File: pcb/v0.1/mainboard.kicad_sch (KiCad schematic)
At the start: 11 parts, among them J1 Conn_01x02_Pin, J2 TYPE_C_Receptacle, J3 Conn_01x04_Pin, U1 AP2112K-3.3TRG1

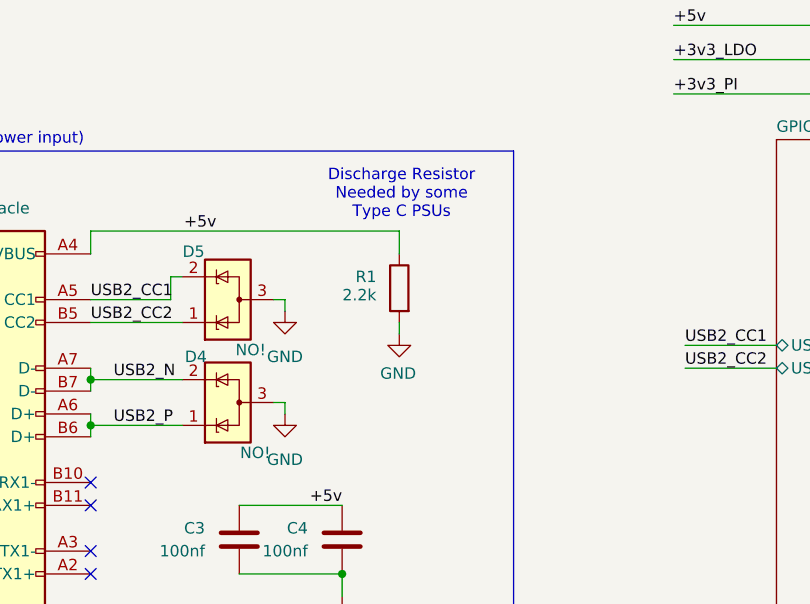
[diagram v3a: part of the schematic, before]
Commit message: Finish ESD protection.
There are now TVS diodes/arrays on both the signal lines and power lines
in every user accessible connector. Such as USBc ports and GPIO.

I have not included them for internal headers, jumpers or connectors
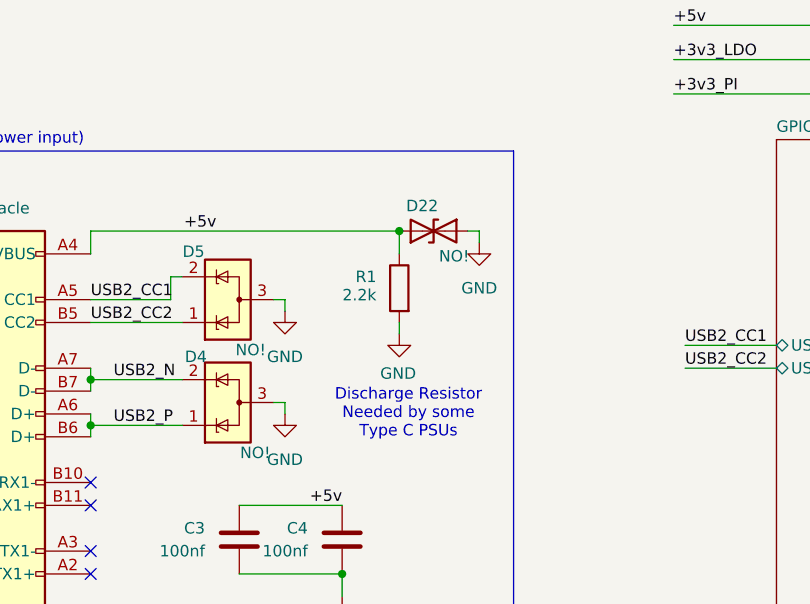
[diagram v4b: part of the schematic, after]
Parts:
- added D22: TVS_DIODE_7.1VC, Diode_SMD:D_SOD-882, symbol TH-1-CC:TVS_DIODE_7.1VC
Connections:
- net +5v: now also D22.1 (A1)
- net GND: now also D22.2 (A2)
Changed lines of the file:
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@@
 	(text "Discharge Resistor\nNeeded by some\nType C PSUs"
 		(exclude_from_sim no)
-		(at 84.074 34.036 0)
+		(at 84.836 58.42 0)
 		(effects
 			(font
@@
 	)
 	(junction
+		(at 83.82 38.1)
+		(diameter 0)
+		(color 0 0 0 0)
+	)
+	(junction
 		(at 281.94 111.76)
 		(diameter 0)
@@
 	(wire
 		(pts
+			(xy 91.44 38.1) (xy 92.71 38.1)
+		)
+		(stroke
+			(width 0)
+			(type default)
+		)
+	)
+	(wire
+		(pts
 			(xy 248.92 64.77) (xy 248.92 74.93)
 		)
@@
 	(wire
 		(pts
+			(xy 92.71 38.1) (xy 92.71 39.37)
+		)
+		(stroke
+			(width 0)
+			(type default)
+		)
+	)
+	(wire
+		(pts
 			(xy 64.77 154.94) (xy 64.77 156.21)
 		)
@@
 					(unit 1)
 				)
+			)
+		)
+	)
+	(symbol
+		(lib_id "TH-1-CC:TVS_DIODE_7.1VC")
+		(at 87.63 38.1 0)
+		(unit 1)
+		(body_style 1)
+		(exclude_from_sim no)
+		(in_bom yes)
+		(on_board yes)
+		(in_pos_files yes)
+		(dnp no)
+		(property "Reference" "D22"
+			(at 86.36 35.306 0)
+			(show_name no)
+			(do_not_autoplace no)
+			(effects
+				(font
+					(size 1.27 1.27)
+				)
+			)
+		)
+		(property "Value" "TVS_DIODE_7.1VC"
+			(at 87.63 31.75 0)
+			(hide yes)
+			(show_name no)
+			(do_not_autoplace no)
+			(effects
+				(font
+					(size 1.27 1.27)
+				)
+			)
+		)
+		(property "Footprint" "Diode_SMD:D_SOD-882"
+			(at 87.63 43.18 0)
+			(hide yes)
+			(show_name no)
+			(do_not_autoplace no)
+			(effects
+				(font
+					(size 1.27 1.27)
+				)
+			)
+		)
+		(property "Datasheet" "https://www.lcsc.com/datasheet/C553450.pdf?spm=wm.sxq.inf.ggs&lcsc_vid=QAILXlUCRldfUlcDQgANV1IDE1JYXwJWRANcAwFRRgAxVlNeRVdYVVNVQFFWVDsOAxUeFF5JWBYZEEoKFBINSQcJGk4NBhADEA4cHktRR1NADxALGw%3D%3D"
+			(at 87.63 38.1 0)
+			(hide yes)
+			(show_name no)
+			(do_not_autoplace no)
+			(effects
+				(font
+					(size 1.27 1.27)
+				)
+			)
+		)
+		(property "Description" "TVS DIODE 5.5VWM 7.1VC DFN1006-2(SOD-882)"
+			(at 87.63 38.1 0)
+			(hide yes)
+			(show_name no)
+			(do_not_autoplace no)
+			(effects
+				(font
+					(size 1.27 1.27)
+				)
+			)
+		)
+		(property "Manufacturer" "Nexperia"
+			(at 87.63 38.1 0)
+			(hide yes)
+			(show_name no)
+			(do_not_autoplace no)
+			(effects
+				(font
+					(size 1.27 1.27)
+				)
+			)
+		)
+		(property "Mfr. Part no." "PTVS5V5D1BLYL"
+			(at 87.63 38.1 0)
+			(hide yes)
+			(show_name no)
+			(do_not_autoplace no)
+			(effects
+				(font
+					(size 1.27 1.27)
+				)
+			)
+		)
+		(property "Distributor DigiKey" "https://www.lcsc.com/product-detail/C553450.html?lcsc_vid=QAILXlUCRldfUlcDQgANV1IDE1JYXwJWRANcAwFRRgAxVlNeRVdYVVNVQFFWVDsOAxUeFF5JWBYZEEoKFBINSQcJGk4NBhADEA4cHktRR1NADxALGw%3D%3D"
+			(at 87.63 38.1 0)
+			(hide yes)
+			(show_name no)
+			(do_not_autoplace no)
+			(effects
+				(font
+					(size 1.27 1.27)
+				)
+			)
+		)
+		(property "LCSC Part no." "C553450"
+			(at 87.63 38.1 0)
+			(hide yes)
+			(show_name no)
+			(do_not_autoplace no)
+			(effects
+				(font
+					(size 1.27 1.27)
+				)
+			)
+		)
+		(property "Stock" "NO!"
+			(at 89.916 40.894 0)
+			(show_name no)
+			(do_not_autoplace no)
+			(effects
+				(font
+					(size 1.27 1.27)
+				)
+			)
+		)
+		(pin "2"
+		)
+		(pin "1"
+		)
+		(instances
+			(project "mainboard"
+				(path "/5b8aa782-5c3d-43e7-a869-3bd000015f52"
+					(reference "D22")
+					(unit 1)
+				)
+			)
+		)
+	)
+	(symbol
+		(lib_id "power:GND")
+		(at 92.71 39.37 0)
+		(unit 1)
+		(body_style 1)
+		(exclude_from_sim no)
+		(in_bom yes)
+		(on_board yes)
+		(in_pos_files yes)
+		(dnp no)
+		(fields_autoplaced yes)
+		(property "Reference" "#PWR070"
+			(at 92.71 45.72 0)
+			(hide yes)
+			(show_name no)
+			(do_not_autoplace no)
+			(effects
+				(font
+					(size 1.27 1.27)
+				)
+			)
+		)
+		(property "Value" "GND"
+			(at 92.71 44.45 0)
+			(show_name no)
+			(do_not_autoplace no)
+			(effects
+				(font
+					(size 1.27 1.27)
+				)
+			)
+		)
+		(property "Footprint" ""
+			(at 92.71 39.37 0)
+			(hide yes)
+			(show_name no)
+			(do_not_autoplace no)
+			(effects
+				(font
+					(size 1.27 1.27)
+				)
+			)
+		)
+		(property "Datasheet" ""
+			(at 92.71 39.37 0)
+			(hide yes)
+			(show_name no)
+			(do_not_autoplace no)
+			(effects
+				(font
+					(size 1.27 1.27)
+				)
+			)
+		)
+		(property "Description" "Power symbol creates a global label with name \"GND\" , ground"
+			(at 92.71 39.37 0)
+			(hide yes)
+			(show_name no)
+			(do_not_autoplace no)
+			(effects
+				(font
+					(size 1.27 1.27)
+				)
+			)
+		)
+		(pin "1"
+		)
+		(instances
+			(project "mainboard"
+				(path "/5b8aa782-5c3d-43e7-a869-3bd000015f52"
+					(reference "#PWR070")
+					(unit 1)
+				)

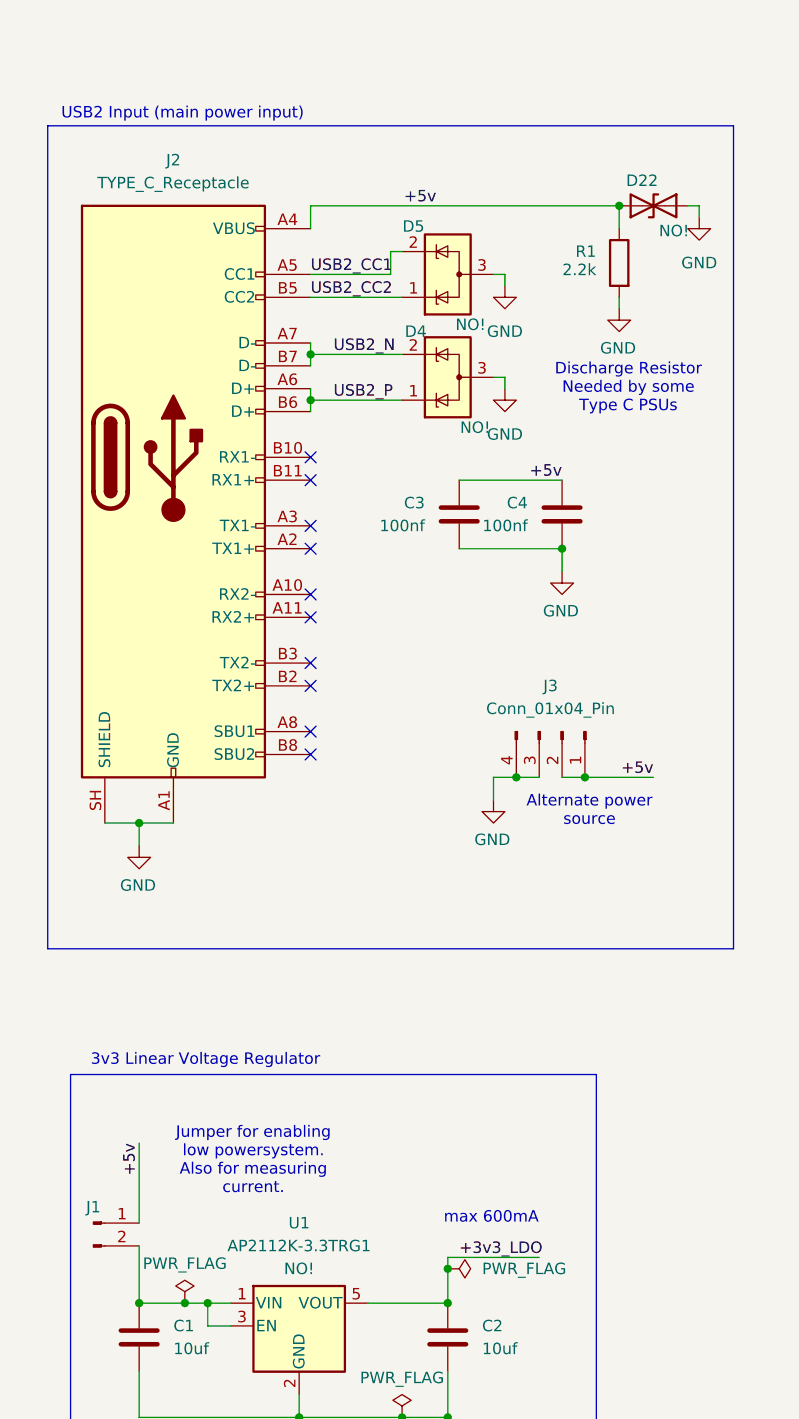
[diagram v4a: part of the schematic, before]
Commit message: Add test points
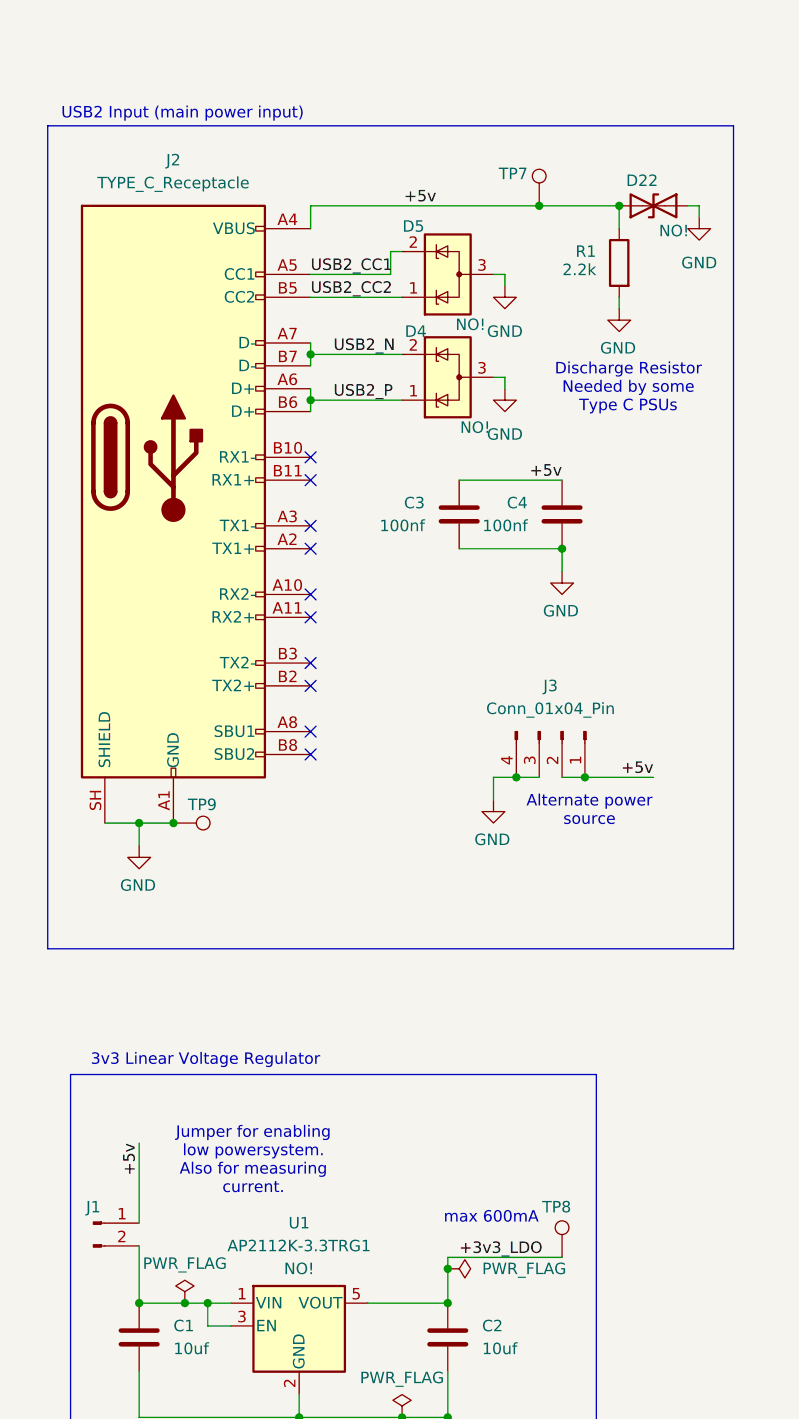
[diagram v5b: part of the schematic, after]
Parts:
- added TP7, TP8, TP9: TestPoint, symbol Connector:TestPoint
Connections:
- net +3v3_LDO: now also TP8.1
- net +5v: now also TP7.1
- net GND: now also TP9.1

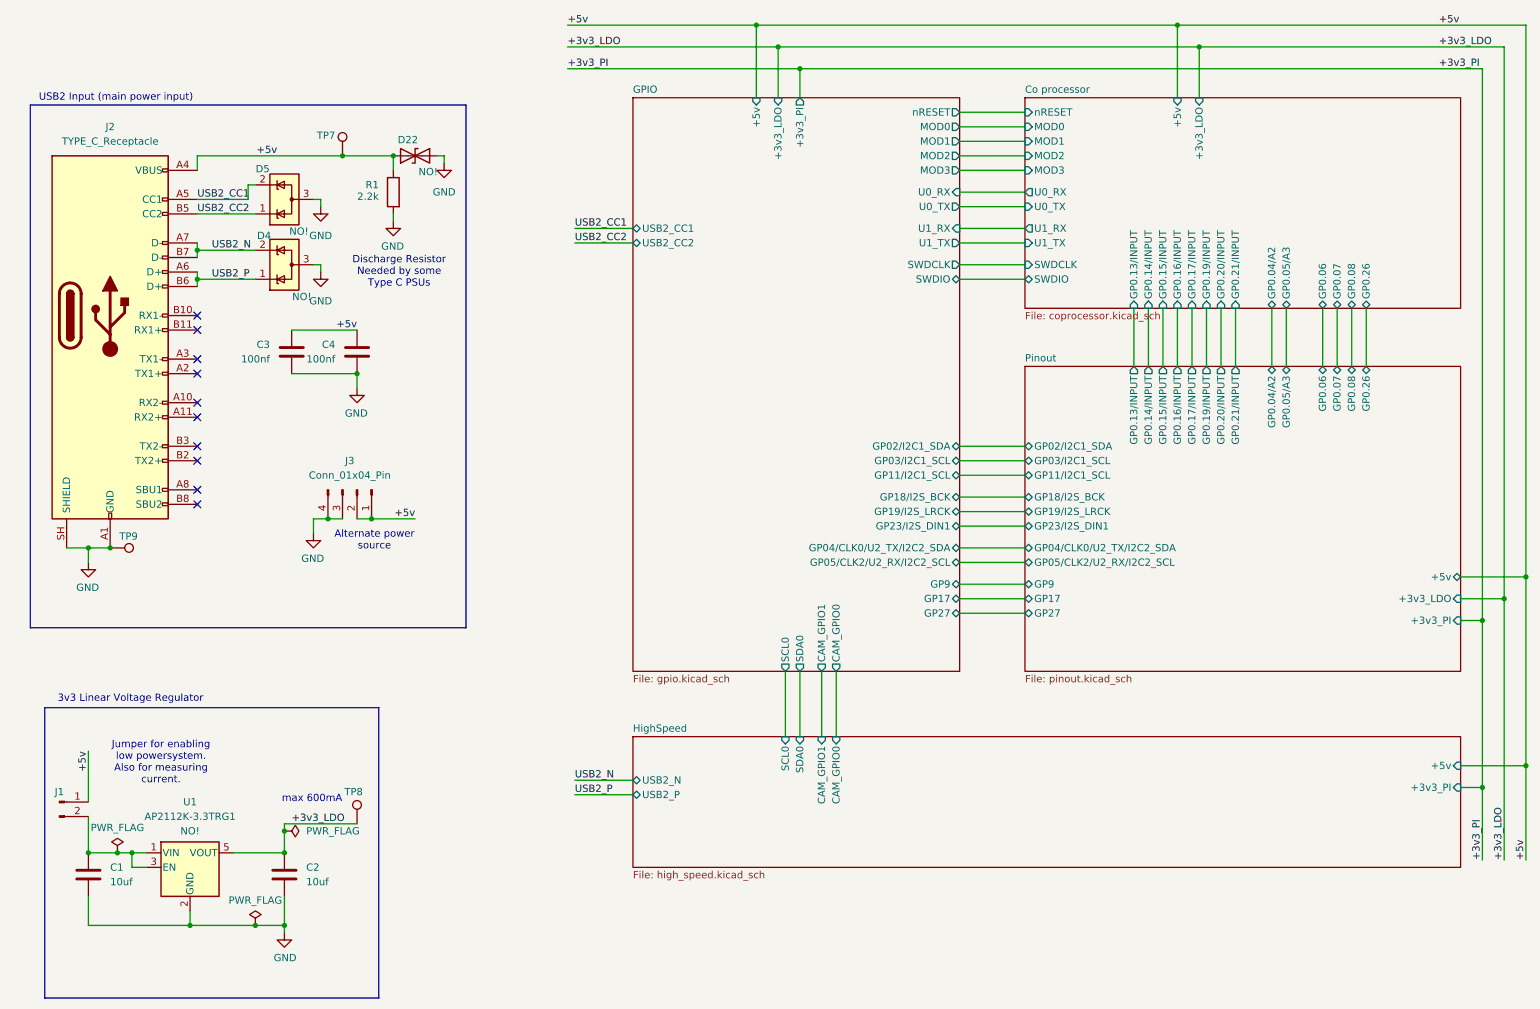
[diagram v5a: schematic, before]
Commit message: Make the ERC happy
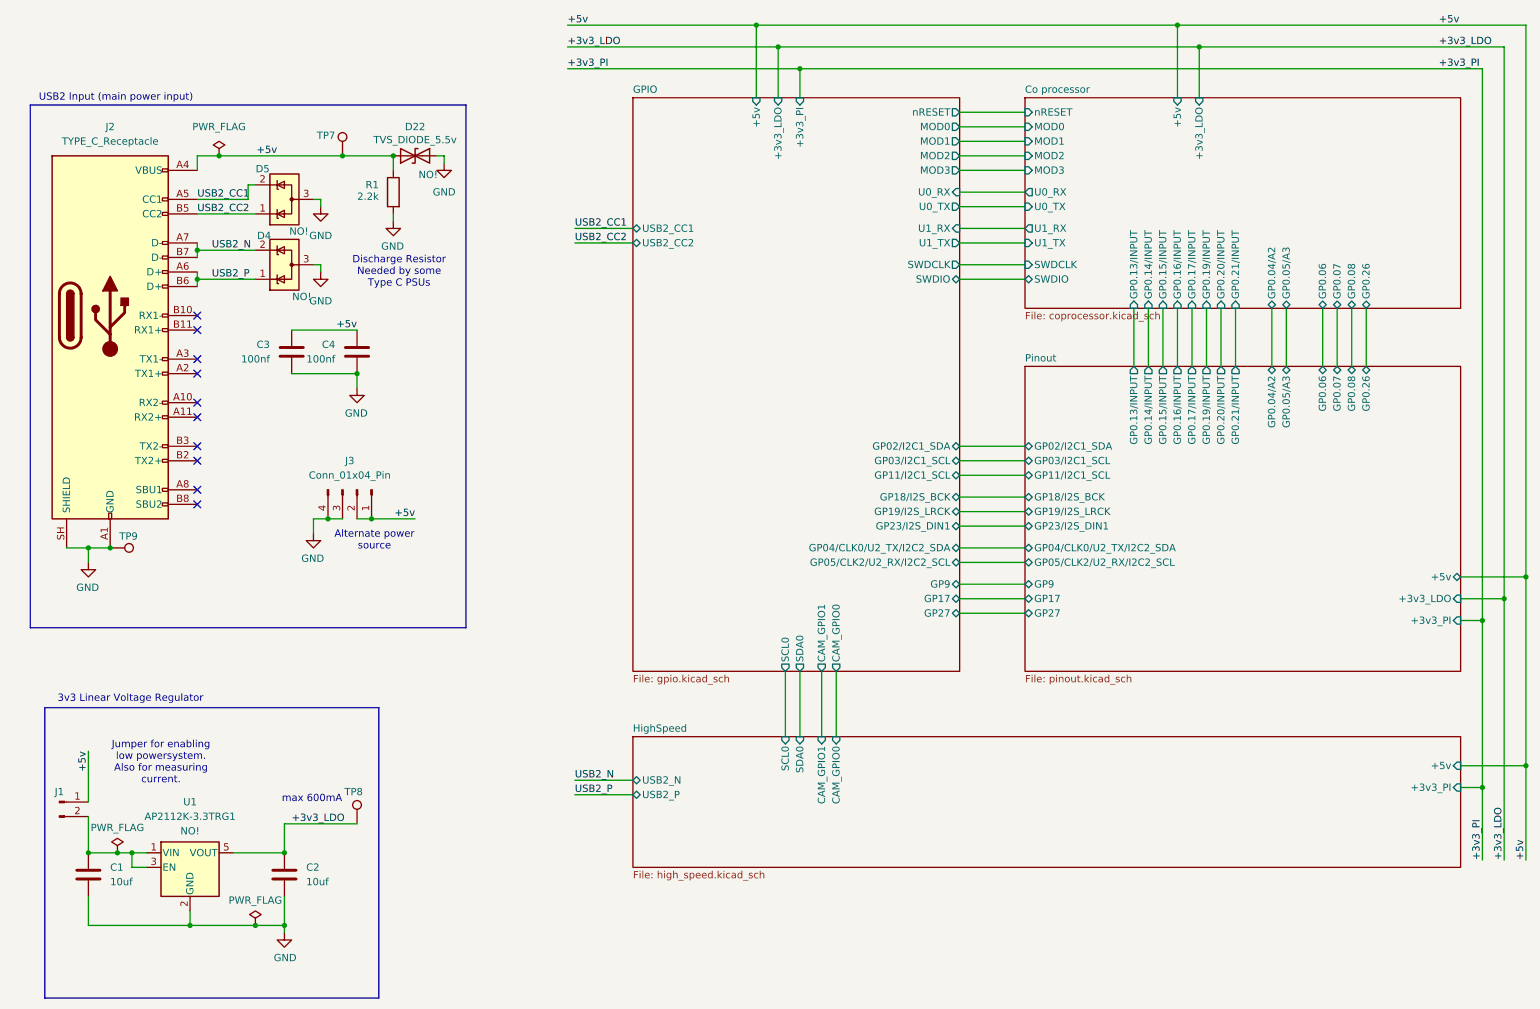
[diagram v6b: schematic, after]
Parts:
- removed D22: TVS_DIODE_7.1VC, Diode_SMD:D_SOD-882, symbol TH-1-CC:TVS_DIODE_7.1VC
- added D22: TVS_DIODE_5.5v, Diode_SMD:D_SOD-882, symbol TH-1-CC:TVS_DIODE_5.5v
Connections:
- net +5v: now also D22.1 (A1)
- net GND: now also D22.2 (A2)
